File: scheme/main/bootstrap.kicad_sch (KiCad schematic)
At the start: 6 parts, among them U1 AM1DS-1515SJZ

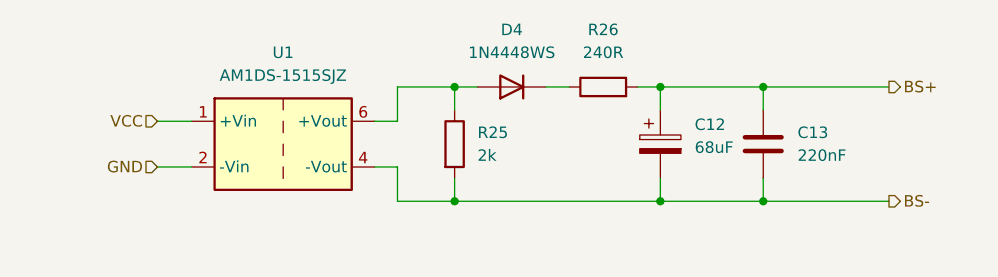
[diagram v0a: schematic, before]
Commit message: removed bootstrap output resistor
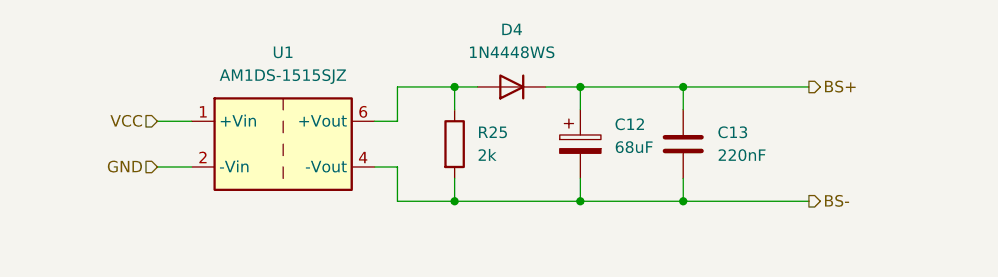
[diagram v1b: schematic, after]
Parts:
- removed R26: 240R, Resistor_SMD:R_0805_2012Metric, symbol Device:R
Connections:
- net BS+: now also D4.1 (K)
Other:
- moved on the sheet: C12, C13
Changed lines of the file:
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@@
 	(paper "A4")
+	(junction
+		(at 118.11 73.66)
+		(diameter 0)
+		(color 0 0 0 0)
+	)
+	(junction
+		(at 129.54 73.66)
+		(diameter 0)
+		(color 0 0 0 0)
+	)
 	(junction
 		(at 104.14 73.66)
@@
 	)
 	(junction
-		(at 138.43 73.66)
+		(at 118.11 86.36)
 		(diameter 0)
 		(color 0 0 0 0)
 	)
 	(junction
-		(at 127 86.36)
-		(diameter 0)
-		(color 0 0 0 0)
-	)
-	(junction
-		(at 138.43 86.36)
+		(at 129.54 86.36)
 		(diameter 0)
 		(color 0 0 0 0)
@@
 		(color 0 0 0 0)
 	)
-	(junction
-		(at 127 73.66)
-		(diameter 0)
-		(color 0 0 0 0)
-	)
-	(wire
-		(pts
-			(xy 138.43 86.36) (xy 152.4 86.36)
-		)
-		(stroke
-			(width 0)
-			(type default)
-		)
-	)
-	(wire
-		(pts
-			(xy 127 83.82) (xy 127 86.36)
+	(wire
+		(pts
+			(xy 129.54 86.36) (xy 143.51 86.36)
+		)
+		(stroke
+			(width 0)
+			(type default)
+		)
+	)
+	(wire
+		(pts
+			(xy 118.11 83.82) (xy 118.11 86.36)
 		)
 		(stroke
@@
 	(wire
 		(pts
-			(xy 138.43 76.2) (xy 138.43 73.66)
+			(xy 129.54 76.2) (xy 129.54 73.66)
 		)
 		(stroke
@@
 	(wire
 		(pts
+			(xy 71.12 82.55) (xy 74.93 82.55)
+		)
+		(stroke
+			(width 0)
+			(type default)
+		)
+	)
+	(wire
+		(pts
 			(xy 97.79 86.36) (xy 104.14 86.36)
 		)
@@
 	(wire
 		(pts
-			(xy 71.12 82.55) (xy 74.93 82.55)
-		)
-		(stroke
-			(width 0)
-			(type default)
-		)
-	)
-	(wire
-		(pts
-			(xy 138.43 73.66) (xy 152.4 73.66)
+			(xy 129.54 73.66) (xy 143.51 73.66)
 		)
 		(stroke
@@
 	(wire
 		(pts
+			(xy 114.3 73.66) (xy 118.11 73.66)
+		)
+		(stroke
+			(width 0)
+			(type default)
+		)
+	)
+	(wire
+		(pts
 			(xy 97.79 77.47) (xy 97.79 73.66)
 		)
@@
 	(wire
 		(pts
-			(xy 127 86.36) (xy 104.14 86.36)
+			(xy 118.11 86.36) (xy 104.14 86.36)
 		)
 		(stroke
@@
 	(wire
 		(pts
-			(xy 138.43 86.36) (xy 127 86.36)
-		)
-		(stroke
-			(width 0)
-			(type default)
-		)
-	)
-	(wire
-		(pts
-			(xy 124.46 73.66) (xy 127 73.66)
+			(xy 129.54 86.36) (xy 118.11 86.36)
+		)
+		(stroke
+			(width 0)
+			(type default)
+		)
+	)
+	(wire
+		(pts
+			(xy 118.11 73.66) (xy 129.54 73.66)
+		)
+		(stroke
+			(width 0)
+			(type default)
+		)
+	)
+	(wire
+		(pts
+			(xy 104.14 83.82) (xy 104.14 86.36)
 		)
 		(stroke
@@
 	(wire
 		(pts
-			(xy 127 73.66) (xy 138.43 73.66)
-		)
-		(stroke
-			(width 0)
-			(type default)
-		)
-	)
-	(wire
-		(pts
-			(xy 114.3 73.66) (xy 116.84 73.66)
-		)
-		(stroke
-			(width 0)
-			(type default)
-		)
-	)
-	(wire
-		(pts
-			(xy 104.14 83.82) (xy 104.14 86.36)
-		)
-		(stroke
-			(width 0)
-			(type default)
-		)
-	)
-	(wire
-		(pts
-			(xy 127 73.66) (xy 127 76.2)
+			(xy 118.11 73.66) (xy 118.11 76.2)
 		)
 		(stroke
@@
 	(wire
 		(pts
-			(xy 138.43 83.82) (xy 138.43 86.36)
+			(xy 129.54 83.82) (xy 129.54 86.36)
 		)
 		(stroke
@@
 	(hierarchical_label "BS-"
 		(shape output)
-		(at 152.4 86.36 0)
+		(at 143.51 86.36 0)
 		(fields_autoplaced yes)
 		(effects
@@
 	(hierarchical_label "BS+"
 		(shape output)
-		(at 152.4 73.66 0)
+		(at 143.51 73.66 0)
 		(fields_autoplaced yes)
 		(effects
@@
 	(symbol
 		(lib_id "Device:C_Polarized")
-		(at 127 80.01 0)
+		(at 118.11 80.01 0)
 		(unit 1)
 		(exclude_from_sim no)
@@
 		(dnp no)
 		(property "Reference" "C12"
-			(at 130.81 77.8509 0)
+			(at 121.92 77.8509 0)
 			(effects
 				(font
@@
 		)
 		(property "Value" "68uF"
-			(at 130.81 80.3909 0)
+			(at 121.92 80.3909 0)
 			(effects
 				(font
@@
 		)
 		(property "Footprint" "Capacitor_SMD:C_Elec_6.3x7.7"
-			(at 127.9652 83.82 0)
+			(at 119.0752 83.82 0)
 			(effects
 				(font
@@
 		)
 		(property "Datasheet" "https://doc.platan.ru/pdf/datasheets/panasonic/FK_V.pdf"
-			(at 127 80.01 0)
+			(at 118.11 80.01 0)
 			(effects
 				(font
@@
 		)
 		(property "Description" "Polarized capacitor"
-			(at 127 80.01 0)
+			(at 118.11 80.01 0)
 			(effects
 				(font
@@
 	(symbol
 		(lib_id "Device:C")
-		(at 138.43 80.01 0)
+		(at 129.54 80.01 0)
 		(unit 1)
 		(exclude_from_sim no)
@@
 		(fields_autoplaced yes)
 		(property "Reference" "C13"
-			(at 142.24 78.7399 0)
+			(at 133.35 78.7399 0)
 			(effects
 				(font
@@
 		)
 		(property "Value" "220nF"
-			(at 142.24 81.2799 0)
+			(at 133.35 81.2799 0)
 			(effects
 				(font
@@
 		)
 		(property "Footprint" "Capacitor_SMD:C_0805_2012Metric"
-			(at 139.3952 83.82 0)
+			(at 130.5052 83.82 0)
 			(effects
 				(font
@@
 		)
 		(property "Datasheet" "~"
-			(at 138.43 80.01 0)
+			(at 129.54 80.01 0)
 			(effects
 				(font
@@
 		)
 		(property "Description" "Unpolarized capacitor"
-			(at 138.43 80.01 0)
+			(at 129.54 80.01 0)
 			(effects
 				(font
@@
 					(unit 1)
 				)
-			)
-		)
-	)
-	(symbol
-		(lib_id "Device:R")
-		(at 120.65 73.66 90)
-		(unit 1)
-		(exclude_from_sim no)
-		(in_bom yes)
-		(on_board yes)
-		(dnp no)
-		(fields_autoplaced yes)
-		(property "Reference" "R26"
-			(at 120.65 67.31 90)
-			(effects
-				(font
-					(size 1.27 1.27)
-				)
-			)
-		)
-		(property "Value" "240R"
-			(at 120.65 69.85 90)
-			(effects
-				(font
-					(size 1.27 1.27)
-				)
-			)
-		)
-		(property "Footprint" "Resistor_SMD:R_0805_2012Metric"
-			(at 120.65 75.438 90)
-			(effects
-				(font
-					(size 1.27 1.27)
-				)
-				(hide yes)
-			)
-		)
-		(property "Datasheet" "~"
-			(at 120.65 73.66 0)
-			(effects
-				(font
-					(size 1.27 1.27)
-				)
-				(hide yes)
-			)
-		)
-		(property "Description" "Resistor"
-			(at 120.65 73.66 0)
-			(effects
-				(font
-					(size 1.27 1.27)
-				)
-				(hide yes)
-			)
-		)
-		(pin "1"
-		)
-		(pin "2"
-		)
-		(instances
-			(project "main"
-				(path "/c11d1dbc-4db9-4712-8d1d-5f6f7086cded/5d407613-ca47-4478-86ea-137e1786be86/32b3c817-68f7-45e1-9258-7a9582664898"
-					(reference "R26")
-					(unit 1)
-				)
-				(path "/c11d1dbc-4db9-4712-8d1d-5f6f7086cded/5d407613-ca47-4478-86ea-137e1786be86/c5b7b692-dec4-4ffa-a62b-cf474dae3f6f"
-					(reference "R30")
-					(unit 1)
-				)
-				(path "/c11d1dbc-4db9-4712-8d1d-5f6f7086cded/5d407613-ca47-4478-86ea-137e1786be86/e7c7cf02-134e-4d37-ae3c-dbc1ef5b400e"
-					(reference "R28")
-					(unit 1)
-				)

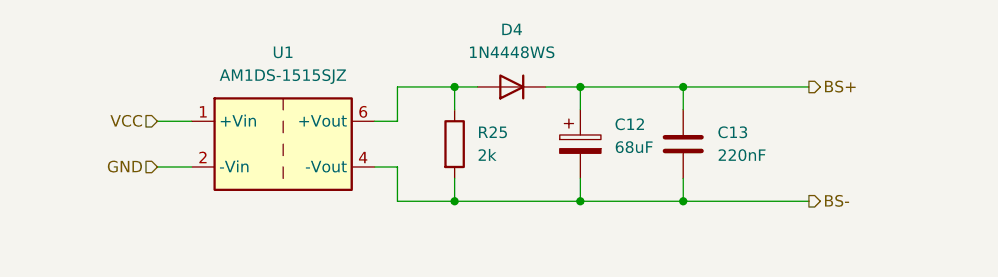
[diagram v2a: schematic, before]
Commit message: bootstrap dc-dc add capacitors & more
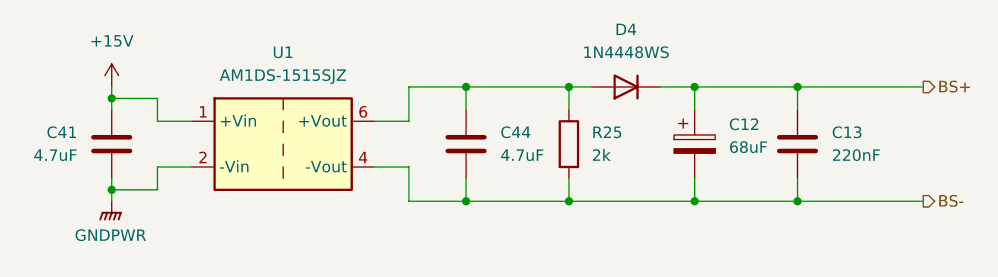
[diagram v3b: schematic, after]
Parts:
- added C41, C44: 4.7uF, Capacitor_SMD:C_0805_2012Metric, symbol Device:C
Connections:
- net BS-: now also C44.2
- net at D4.2 (A), R25.1, U1.6 (+Vout): now also C44.1
- net GND renamed GNDPWR
- net GNDPWR: now also C41.2
- net VCC renamed +15V
- net +15V: now also C41.1
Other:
- moved on the sheet: C12, C13, D4, R25

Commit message: power scheme in progress (added dc-dc)
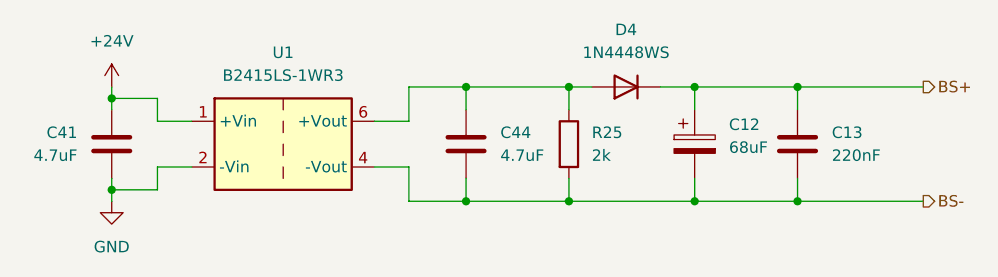
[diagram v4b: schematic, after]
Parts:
- removed U1: AM1DS-1515SJZ, Converter_DCDC:Converter_DCDC_TRACO_TMA-15xxS_24xxS_Single_THT, symbol Converter_DCDC:TMA-1515S
- added U1: B2415LS-1WR3, Converter_DCDC:Converter_DCDC_TRACO_TMA-15xxS_24xxS_Single_THT, symbol main:B2415LS-1WR3
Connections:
- net BS-: now also U1.4 (-Vout)
- net at C44.1, D4.2 (A), R25.1: now also U1.6 (+Vout)
- net +15V renamed +24V
- net +24V: now also U1.1 (+Vin)
- net GNDPWR renamed GND
- net GND: now also U1.2 (-Vin)
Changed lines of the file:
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@@
 	)
 	(symbol
-		(lib_id "Converter_DCDC:TMA-1515S")
+		(lib_id "main:B2415LS-1WR3")
 		(at 85.09 80.01 0)
 		(unit 1)
@@
 			)
 		)
-		(property "Value" "AM1DS-1515SJZ"
+		(property "Value" "B2415LS-1WR3"
 			(at 85.09 72.39 0)
 			(effects
@@
 			)
 		)
-		(property "Datasheet" "https://doc.platan.ru/pdf/datasheets/aimtec/AM1DS-JZ.pdf"
+		(property "Datasheet" "https://www.compel.ru/item-pdf/2ec1768d3564db0bf47544ec3d83c3f2/ps/mornsun~a_s-1wr3---b_ls-1wr3.pdf"
 			(at 85.09 86.36 0)
 			(effects
@@
 			)
 		)
-		(property "Description" "AM1DS-1515SJZ, DC/DC, 1Вт, вх.13.5:16.5В, вых.15В/0.007:0.067А, SIP7"
+		(property "Description" "1W DC/DC converter unregulated, 21.6-26.4V input, 15V fixed output voltage, 67mA output, 1.5kVDC isolation, SIP-7"
 			(at 85.09 80.01 0)
 			(effects
@@
 			)
 		)
+		(pin "4"
+		)
+		(pin "1"
+		)
+		(pin "6"
+		)
 		(pin "2"
 		)
-		(pin "4"
-		)
-		(pin "6"
-		)
-		(pin "1"
-		)
-		(instances
-			(project "main"
+		(instances
+			(project ""
 				(path "/c11d1dbc-4db9-4712-8d1d-5f6f7086cded/5d407613-ca47-4478-86ea-137e1786be86/32b3c817-68f7-45e1-9258-7a9582664898"
 					(reference "U1")
@@
 	)
 	(symbol
-		(lib_id "power:GNDPWR")
-		(at 66.04 86.36 0)
-		(unit 1)
-		(exclude_from_sim no)
-		(in_bom yes)
-		(on_board yes)
-		(dnp no)
-		(fields_autoplaced yes)
-		(property "Reference" "#PWR39"
-			(at 66.04 91.44 0)
-			(effects
-				(font
-					(size 1.27 1.27)
-				)
-				(hide yes)
-			)
-		)
-		(property "Value" "GNDPWR"
-			(at 65.913 90.17 0)
-			(effects
-				(font
-					(size 1.27 1.27)
-				)
-			)
-		)
-		(property "Footprint" ""
-			(at 66.04 87.63 0)
-			(effects
-				(font
-					(size 1.27 1.27)
-				)
-				(hide yes)
-			)
-		)
-		(property "Datasheet" ""
-			(at 66.04 87.63 0)
-			(effects
-				(font
-					(size 1.27 1.27)
-				)
-				(hide yes)
-			)
-		)
-		(property "Description" "Power symbol creates a global label with name \"GNDPWR\" , global ground"
-			(at 66.04 86.36 0)
-			(effects
-				(font
-					(size 1.27 1.27)
-				)
-				(hide yes)
-			)
-		)
-		(pin "1"
-		)
-		(instances
-			(project ""
-				(path "/c11d1dbc-4db9-4712-8d1d-5f6f7086cded/5d407613-ca47-4478-86ea-137e1786be86/32b3c817-68f7-45e1-9258-7a9582664898"
-					(reference "#PWR39")
-					(unit 1)
-				)
-				(path "/c11d1dbc-4db9-4712-8d1d-5f6f7086cded/5d407613-ca47-4478-86ea-137e1786be86/c5b7b692-dec4-4ffa-a62b-cf474dae3f6f"
-					(reference "#PWR41")
-					(unit 1)
-				)
-				(path "/c11d1dbc-4db9-4712-8d1d-5f6f7086cded/5d407613-ca47-4478-86ea-137e1786be86/e7c7cf02-134e-4d37-ae3c-dbc1ef5b400e"
-					(reference "#PWR40")
-					(unit 1)
-				)
-			)
-		)
-	)
-	(symbol
 		(lib_id "Diode:1N4448WS")
 		(at 123.19 73.66 180)
@@
 	)
 	(symbol
-		(lib_id "power:+15V")
+		(lib_id "power:GND")
+		(at 66.04 86.36 0)
+		(unit 1)
+		(exclude_from_sim no)
+		(in_bom yes)
+		(on_board yes)
+		(dnp no)
+		(fields_autoplaced yes)
+		(property "Reference" "#PWR39"
+			(at 66.04 92.71 0)
+			(effects
+				(font
+					(size 1.27 1.27)
+				)
+				(hide yes)
+			)
+		)
+		(property "Value" "GND"
+			(at 66.04 91.44 0)
+			(effects
+				(font
+					(size 1.27 1.27)
+				)
+			)
+		)
+		(property "Footprint" ""
+			(at 66.04 86.36 0)
+			(effects
+				(font
+					(size 1.27 1.27)
+				)
+				(hide yes)
+			)
+		)
+		(property "Datasheet" ""
+			(at 66.04 86.36 0)
+			(effects
+				(font
+					(size 1.27 1.27)
+				)
+				(hide yes)
+			)
+		)
+		(property "Description" "Power symbol creates a global label with name \"GND\" , ground"
+			(at 66.04 86.36 0)
+			(effects
+				(font
+					(size 1.27 1.27)
+				)
+				(hide yes)
+			)
+		)
+		(pin "1"
+		)
+		(instances
+			(project ""
+				(path "/c11d1dbc-4db9-4712-8d1d-5f6f7086cded/5d407613-ca47-4478-86ea-137e1786be86/32b3c817-68f7-45e1-9258-7a9582664898"
+					(reference "#PWR39")
+					(unit 1)
+				)
+				(path "/c11d1dbc-4db9-4712-8d1d-5f6f7086cded/5d407613-ca47-4478-86ea-137e1786be86/c5b7b692-dec4-4ffa-a62b-cf474dae3f6f"
+					(reference "#PWR41")
+					(unit 1)
+				)
+				(path "/c11d1dbc-4db9-4712-8d1d-5f6f7086cded/5d407613-ca47-4478-86ea-137e1786be86/e7c7cf02-134e-4d37-ae3c-dbc1ef5b400e"
+					(reference "#PWR40")
+					(unit 1)
+				)
+			)
+		)
+	)
+	(symbol
+		(lib_id "power:+24V")
 		(at 66.04 73.66 0)
 		(unit 1)
@@
 			)
 		)
-		(property "Value" "+15V"
+		(property "Value" "+24V"
 			(at 66.04 68.58 0)
 			(effects
@@
 			)
 		)
-		(property "Description" "Power symbol creates a global label with name \"+15V\""
+		(property "Description" "Power symbol creates a global label with name \"+24V\""
 			(at 66.04 73.66 0)
 			(effects

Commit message: power scheme
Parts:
- C12: value 68uF -> 47uF; footprint Capacitor_SMD:C_Elec_6.3x7.7 -> Capacitor_SMD:C_Elec_5x5.8
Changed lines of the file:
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@@
 		(shape output)
 		(at 156.21 86.36 0)
+		(fields_autoplaced yes)
 		(effects
 			(font
@@
 		(shape output)
 		(at 156.21 73.66 0)
+		(fields_autoplaced yes)
 		(effects
 			(font
@@
 		(dnp no)
 		(property "Reference" "C12"
-			(at 134.62 77.8509 0)
+			(at 134.366 78.74 0)
 			(effects
 				(font
@@
 			)
 		)
-		(property "Value" "68uF"
-			(at 134.62 80.3909 0)
+		(property "Value" "47uF"
+			(at 134.366 81.28 0)
 			(effects
 				(font
@@
 			)
 		)
-		(property "Footprint" "Capacitor_SMD:C_Elec_6.3x7.7"
+		(property "Footprint" "Capacitor_SMD:C_Elec_5x5.8"
 			(at 131.7752 83.82 0)
 			(effects
@@
 			)
 		)
-		(property "Datasheet" "https://doc.platan.ru/pdf/datasheets/panasonic/FK_V.pdf"
+		(property "Datasheet" "https://www.platan.ru/cgi-bin/qwery.pl/id=2015355001"
 			(at 130.81 80.01 0)
 			(effects
